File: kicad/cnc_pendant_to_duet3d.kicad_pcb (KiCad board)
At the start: 2 copper layers, 60 x 34 mm, 9 parts, among them J1 Conn_01x04_Male, J2 DA15_Socket_MountingHoles, U1 Sparkfun_Pro_Micro

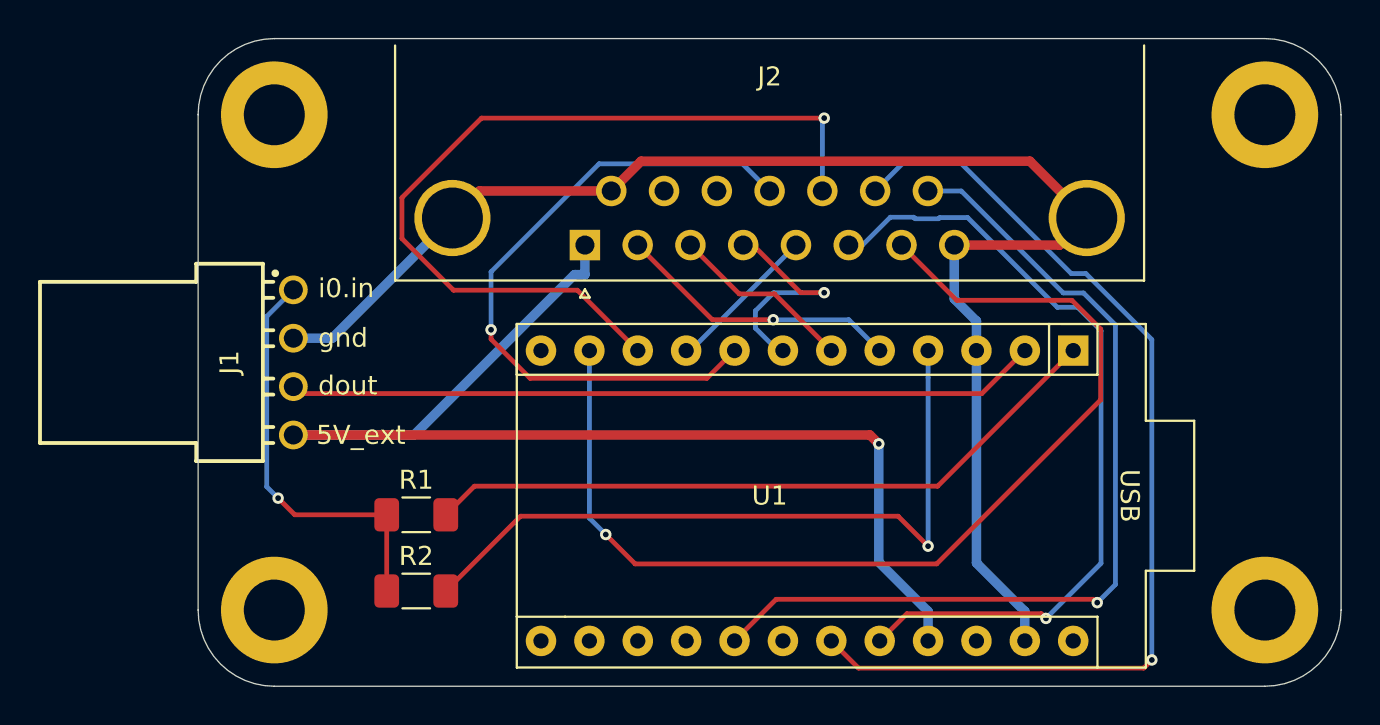
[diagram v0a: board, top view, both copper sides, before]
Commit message: Switched to global labels in schematic. Updated PCB
Not tested
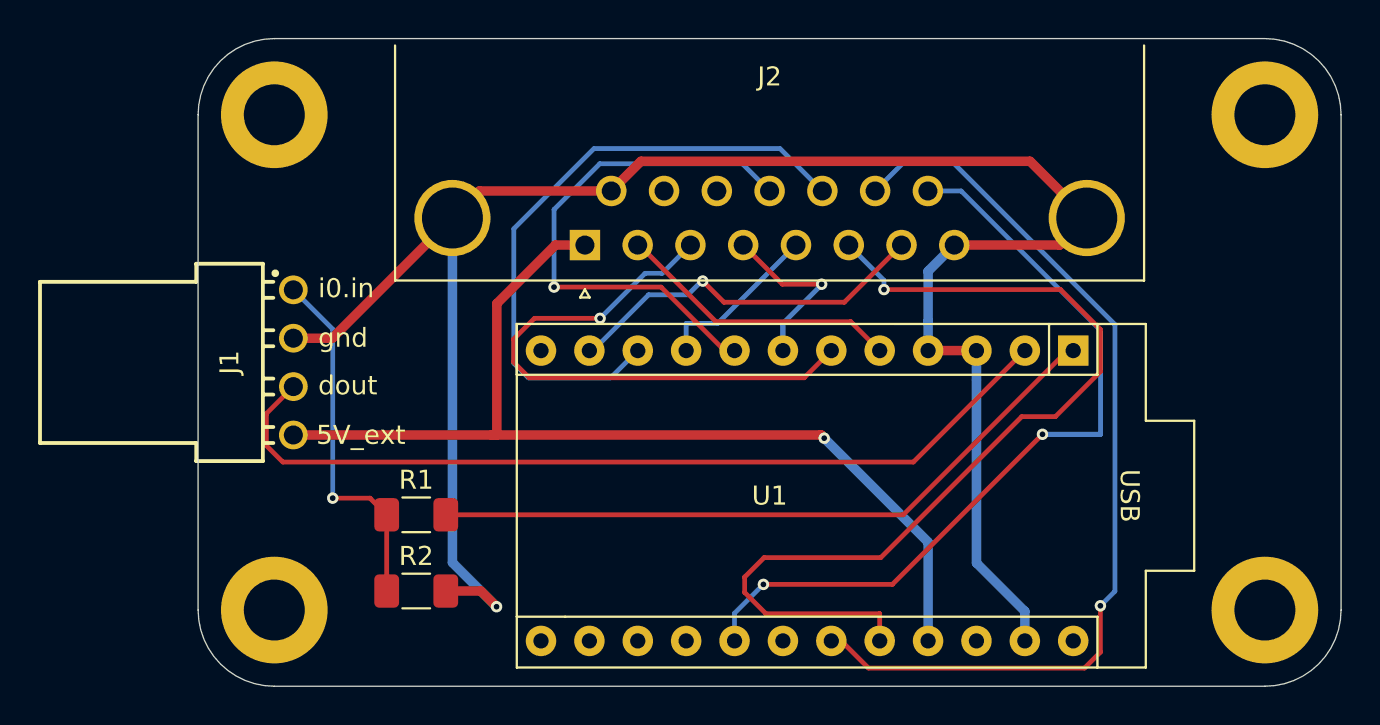
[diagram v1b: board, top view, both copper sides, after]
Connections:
- net /4TH_AXIS renamed 4TH_AXIS
- net /5TH_AXIS renamed 5TH_AXIS
- net /A renamed A
- net /B renamed B
- net /DOUT renamed RXI
- net /LED renamed LED+
- net /STOP renamed STOP
- net /X1 renamed X1
- net /X10 renamed X10
- net /X100 renamed X100
- net /X_AXIS renamed X_AXIS
- net /Y_AXIS renamed Y_AXIS
- net /Z_AXIS renamed Z_AXIS
- R2 pad 2: Net-(R2-Pad2) -> GND
- U1 pad 12: unconnected-(U1-9-Pad12) -> 6TH_AXIS
- U1 pad 4: Net-(R2-Pad2) -> GND
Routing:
- net Net-(R2-Pad2): track 37.9 -> 0.00 mm, vias 1 -> 0
- net 5TH_AXIS: track 56.2 -> 20.0 mm
- net GND: track 76.6 -> 103.6 mm, vias 0 -> 1
- net B: track 9.69 -> 30.1 mm, vias 0 -> 1
- net 4TH_AXIS: track 44.7 -> 33.3 mm, vias 1 -> 0
- net X100: track 42.1 -> 50.5 mm
- net +5V: track 62.7 -> 54.6 mm
- net Y_AXIS: track 35.3 -> 27.8 mm
- net RXI: track 39.5 -> 46.3 mm
- net X10: track 53.4 -> 49.3 mm
- net /io0.in: track 21.8 -> 19.0 mm
- net STOP: track 47.7 -> 45.2 mm, vias 1 -> 2
- net X_AXIS: track 12.1 -> 10.7 mm
- net Z_AXIS: track 8.06 -> 8.90 mm
- net A: vias 1 -> 0

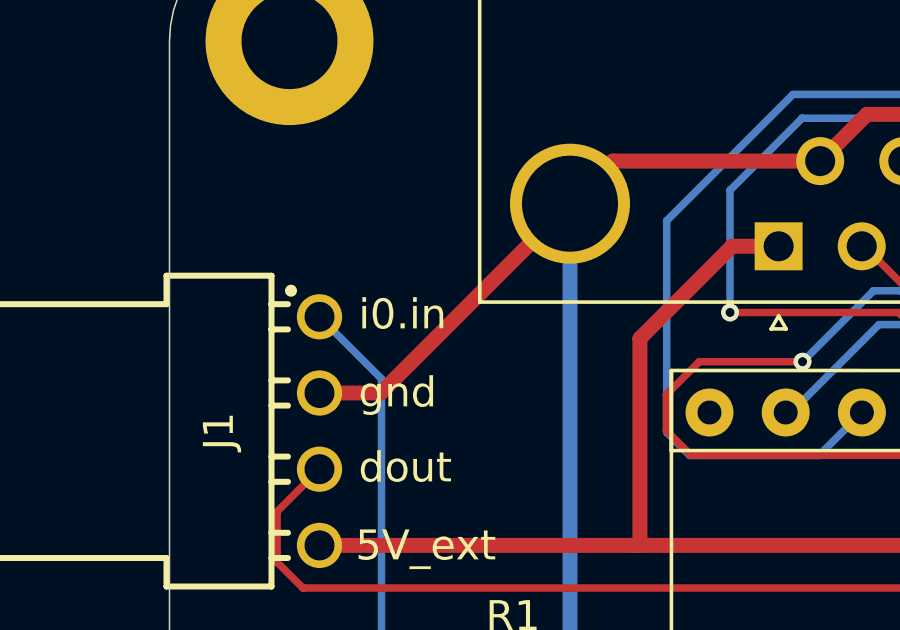
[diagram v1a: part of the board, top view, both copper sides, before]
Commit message: Corrected i0.in to io0.in on silkscreen
Regenerated production files
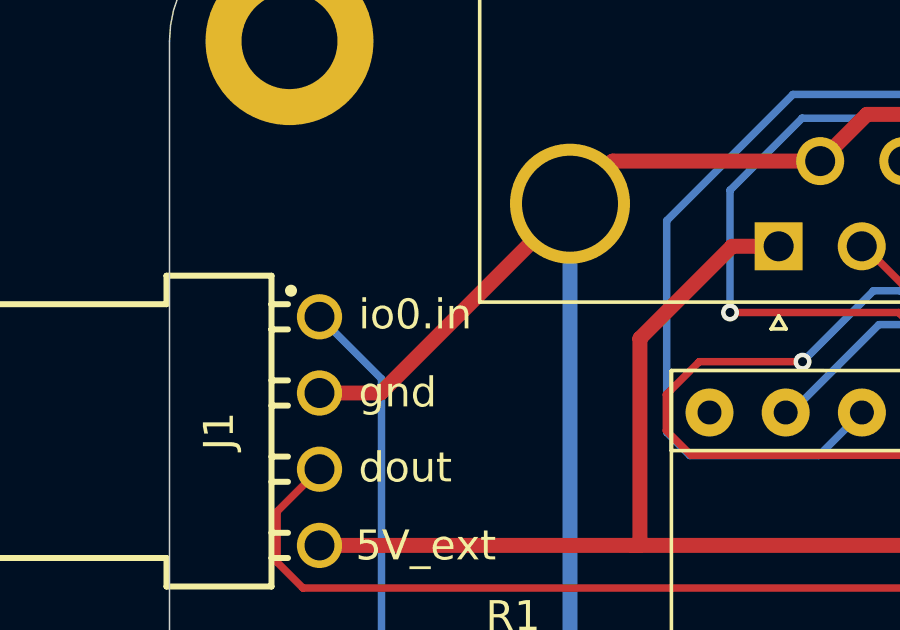
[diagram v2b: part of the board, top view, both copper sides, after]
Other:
- board text added: "io0.in"
- board text added: "io0.in/urxd0"
- board text removed: "i0.in"
- board text removed: "i0.in/urxd0"
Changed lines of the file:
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@@
 		)
 	)
-	(gr_text "i0.in"
+	(gr_text "io0.in"
 		(at 127.3 79.7 0)
 		(layer "F.SilkS")
@@
 		)
 	)
-	(gr_text "i0.in/urxd0"
+	(gr_text "io0.in/urxd0"
 		(at 126.9 79.8 0)
 		(layer "B.SilkS")
